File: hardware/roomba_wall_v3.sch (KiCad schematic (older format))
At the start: 15 parts, among them CON1 AVR-ISP-6, IC1 MIC5225-3.3, J1 USB_OTG, J2 JSTPH, J3 JSTPH, Q1 Q_NPN_BEC, U1 ATTINY45-20SU, Y1 8Mhz

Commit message: Schematic for v3 Added a user button mostly Changed to a switch and a battery, like v2 (from Christmas Barrier)
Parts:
- removed C1: 10uF, lib_fp:C_1206, symbol C
- removed IC1: MIC5225-3.3, lib_fp:SOT-23-5_HandSoldering, symbol MIC5225-3.3
- removed J1: USB_OTG, lib_fp:USB_Micro-B_10103594-0001LF, symbol USB_OTG
- removed J3: JSTPH, lib_fp:JST_PH_B2B-PH-SM4-TB_02x2.00mm_Straight, symbol Conn_01x02
- added BT?: Battery_Cell, symbol Battery_Cell
- added R?: 10k, symbol R
- added SW?: On/Off, symbol SW_SPDT
- added SW?: Button, symbol SW_Push
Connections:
- net labels added: SCK/BUTTON, VBAT
- net labels removed: SCK, VBUS
- wire segments 49 -> 40
- no-connect marks 4 -> 1

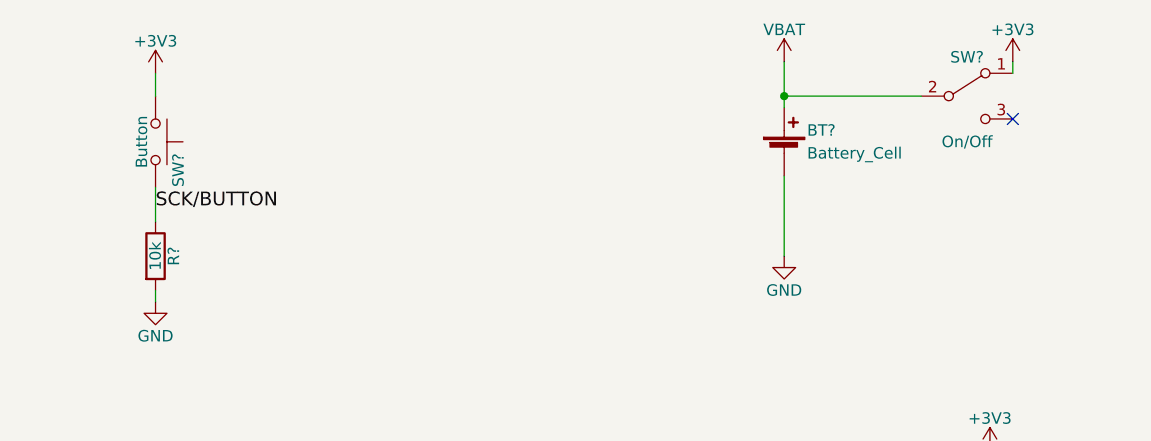
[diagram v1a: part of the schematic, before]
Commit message: Progress on annotating and reassigning footprints I want to use 0805, since they seem the easiest and cheapest to source
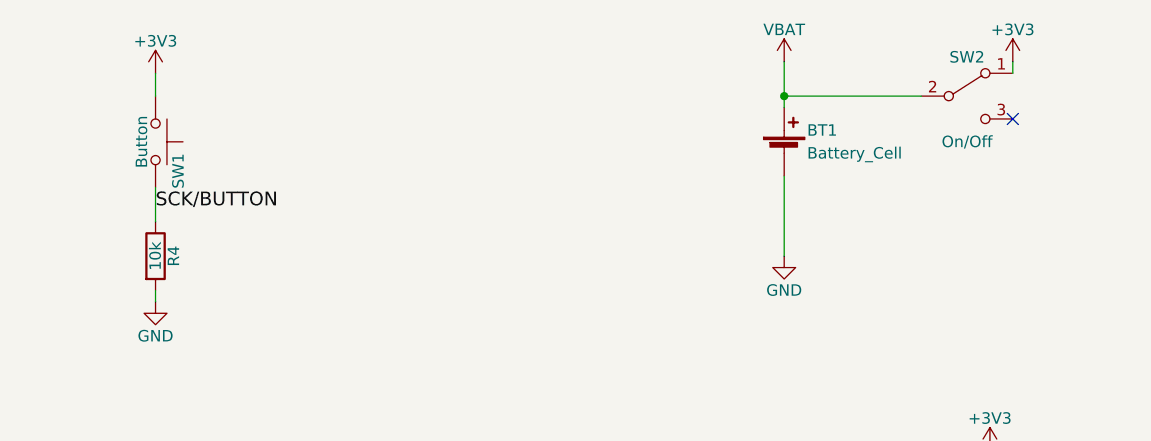
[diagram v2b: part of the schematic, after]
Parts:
- C2: footprint lib_fp:C_1206 -> Capacitors_SMD:C_0805
- D1: footprint lib_fp:LED_1206 -> LEDs:LED_0805
- D2: footprint lib_fp:LED_0603_HandSoldering -> LEDs:LED_0603
- Q1: footprint lib_fp:SOT-23_Handsoldering -> TO_SOT_Packages_SMD:SOT-23
- R1, R2, R3: footprint lib_fp:R_1206 -> Resistors_SMD:R_0805
- R4: renamed from R?; footprint (none) -> Resistors_SMD:R_0805
- gave numbers to parts that had none: 3
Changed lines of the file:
@@
 LIBS:contrib
 LIBS:valves
-LIBS:petezah
-LIBS:petezah-conn
-LIBS:petezah-devices
-LIBS:petezah-ic
-LIBS:petezah-jumpers
-LIBS:petezah-power
-LIBS:roomba_wall_v3-cache
 EELAYER 25 0
 EELAYER END
@@
 RST
 $Comp
-L GND #PWR01
+L GND #PWR10
 U 1 1 5A1C62BB
 P 7300 4100
-F 0 "#PWR01" H 7300 3850 50  0001 C CNN
+F 0 "#PWR10" H 7300 3850 50  0001 C CNN
 F 1 "GND" H 7300 3950 50  0000 C CNN
 F 2 "" H 7300 4100 50  0001 C CNN
@@
 $EndComp
 $Comp
-L +3V3 #PWR02
+L +3V3 #PWR9
 U 1 1 5A1C6304
 P 7300 3200
-F 0 "#PWR02" H 7300 3050 50  0001 C CNN
+F 0 "#PWR9" H 7300 3050 50  0001 C CNN
 F 1 "+3V3" H 7300 3340 50  0000 C CNN
 F 2 "" H 7300 3200 50  0001 C CNN
@@
 $EndComp
 $Comp
-L GND #PWR03
+L GND #PWR6
 U 1 1 5A1C63A0
 P 3950 4350
-F 0 "#PWR03" H 3950 4100 50  0001 C CNN
+F 0 "#PWR6" H 3950 4100 50  0001 C CNN
 F 1 "GND" H 3950 4200 50  0000 C CNN
 F 2 "" H 3950 4350 50  0001 C CNN
@@
 F 0 "R1" V 1330 3550 50  0000 C CNN
 F 1 "560" V 1250 3550 50  0000 C CNN
-F 2 "lib_fp:R_1206" V 1180 3550 50  0001 C CNN
+F 2 "Resistors_SMD:R_0805" V 1180 3550 50  0001 C CNN
 F 3 "" H 1250 3550 50  0001 C CNN
 	1    1250 3550
@@
 F 0 "R2" V 2030 3550 50  0000 C CNN
 F 1 "560" V 1950 3550 50  0000 C CNN
-F 2 "lib_fp:R_1206" V 1880 3550 50  0001 C CNN
+F 2 "Resistors_SMD:R_0805" V 1880 3550 50  0001 C CNN
 F 3 "" H 1950 3550 50  0001 C CNN
 	1    1950 3550
@@
 F 0 "R3" V 2530 3550 50  0000 C CNN
 F 1 "51" V 2450 3550 50  0000 C CNN
-F 2 "lib_fp:R_1206" V 2380 3550 50  0001 C CNN
+F 2 "Resistors_SMD:R_0805" V 2380 3550 50  0001 C CNN
 F 3 "" H 2450 3550 50  0001 C CNN
 	1    2450 3550
@@
 F 0 "D1" H 1250 4300 50  0000 C CNN
 F 1 "LED" H 1250 4100 50  0000 C CNN
-F 2 "lib_fp:LED_1206" H 1250 4200 50  0001 C CNN
+F 2 "LEDs:LED_0805" H 1250 4200 50  0001 C CNN
 F 3 "" H 1250 4200 50  0001 C CNN
 	1    1250 4200
@@
 F 0 "D2" H 2450 4000 50  0000 C CNN
 F 1 "IR_LED" H 2450 3800 50  0000 C CNN
-F 2 "lib_fp:LED_0603_HandSoldering" H 2450 3900 50  0001 C CNN
+F 2 "LEDs:LED_0603" H 2450 3900 50  0001 C CNN
 F 3 "" H 2450 3900 50  0001 C CNN
 	1    2450 3900
@@
 $EndComp
 $Comp
-L +3V3 #PWR04
+L +3V3 #PWR2
 U 1 1 5A1C6749
 P 2450 3100
-F 0 "#PWR04" H 2450 2950 50  0001 C CNN
+F 0 "#PWR2" H 2450 2950 50  0001 C CNN
 F 1 "+3V3" H 2450 3240 50  0000 C CNN
 F 2 "" H 2450 3100 50  0001 C CNN
@@
 $EndComp
 $Comp
-L GND #PWR05
+L GND #PWR1
 U 1 1 5A1C676D
 P 1250 4700
-F 0 "#PWR05" H 1250 4450 50  0001 C CNN
+F 0 "#PWR1" H 1250 4450 50  0001 C CNN
 F 1 "GND" H 1250 4550 50  0000 C CNN
 F 2 "" H 1250 4700 50  0001 C CNN
@@
 $EndComp
 $Comp
-L GND #PWR06
+L GND #PWR3
 U 1 1 5A1C6791
 P 2450 4700
-F 0 "#PWR06" H 2450 4450 50  0001 C CNN
+F 0 "#PWR3" H 2450 4450 50  0001 C CNN
 F 1 "GND" H 2450 4550 50  0000 C CNN
 F 2 "" H 2450 4700 50  0001 C CNN
@@
 RST
 $Comp
-L +3V3 #PWR07
+L +3V3 #PWR15
 U 1 1 5A1C7024
 P 9800 3200
-F 0 "#PWR07" H 9800 3050 50  0001 C CNN
+F 0 "#PWR15" H 9800 3050 50  0001 C CNN
 F 1 "+3V3" H 9800 3340 50  0000 C CNN
 F 2 "" H 9800 3200 50  0001 C CNN
@@
 $EndComp
 $Comp
-L GND #PWR08
+L GND #PWR16
 U 1 1 5A1C704A
 P 9800 4100
-F 0 "#PWR08" H 9800 3850 50  0001 C CNN
+F 0 "#PWR16" H 9800 3850 50  0001 C CNN
 F 1 "GND" H 9800 3950 50  0000 C CNN
 F 2 "" H 9800 4100 50  0001 C CNN
@@
 F 0 "C2" H 7675 3700 50  0000 L CNN
 F 1 "10uF" H 7675 3500 50  0000 L CNN
-F 2 "lib_fp:C_1206" H 7688 3450 50  0001 C CNN
+F 2 "Capacitors_SMD:C_0805" H 7688 3450 50  0001 C CNN
 F 3 "" H 7650 3600 50  0001 C CNN
 	1    7650 3600
@@
 $EndComp
 $Comp
-L GND #PWR013
+L GND #PWR12
 U 1 1 5A1C763D
 P 7650 3750
-F 0 "#PWR013" H 7650 3500 50  0001 C CNN
+F 0 "#PWR12" H 7650 3500 50  0001 C CNN
 F 1 "GND" H 7650 3600 50  0000 C CNN
 F 2 "" H 7650 3750 50  0001 C CNN
@@
 $EndComp
 $Comp
-L +3V3 #PWR017
+L +3V3 #PWR13
 U 1 1 5A1C8097
 P 8400 1550
-F 0 "#PWR017" H 8400 1400 50  0001 C CNN
+F 0 "#PWR13" H 8400 1400 50  0001 C CNN
 F 1 "+3V3" H 8400 1690 50  0000 C CNN
 F 2 "" H 8400 1550 50  0001 C CNN
@@
 $EndComp
 $Comp
-L GND #PWR019
+L GND #PWR14
 U 1 1 5A1C86A4
 P 8400 2350
-F 0 "#PWR019" H 8400 2100 50  0001 C CNN
+F 0 "#PWR14" H 8400 2100 50  0001 C CNN
 F 1 "GND" H 8400 2200 50  0000 C CNN
 F 2 "" H 8400 2350 50  0001 C CNN
@@
 F 0 "Q1" H 2550 4400 50  0000 L CNN
 F 1 "Q_NPN_BEC" H 2550 4300 50  0000 L CNN
-F 2 "lib_fp:SOT-23_Handsoldering" H 2550 4450 50  0001 C CNN
+F 2 "TO_SOT_Packages_SMD:SOT-23" H 2550 4450 50  0001 C CNN
 F 3 "" H 2350 4350 50  0001 C CNN
 	1    2350 4350
@@
 $EndComp
 $Comp
-L Battery_Cell BT?
+L Battery_Cell BT1
 U 1 1 5A96233E
 P 6400 1900
-F 0 "BT?" H 6500 2000 50  0000 L CNN
+F 0 "BT1" H 6500 2000 50  0000 L CNN
 F 1 "Battery_Cell" H 6500 1900 50  0000 L CNN
 F 2 "" V 6400 1960 50  0001 C CNN
@@
 $EndComp
 $Comp
-L VBAT #PWR?
+L VBAT #PWR7
 U 1 1 5A96243B
 P 6400 1500
-F 0 "#PWR?" H 6400 1350 50  0001 C CNN
+F 0 "#PWR7" H 6400 1350 50  0001 C CNN
 F 1 "VBAT" H 6400 1640 50  0000 C CNN
 F 2 "" H 6400 1500 50  0000 C CNN
@@
 	6400 1500 6400 1700
 $Comp
-L GND #PWR?
+L GND #PWR8
 U 1 1 5A962497
 P 6400 2350
-F 0 "#PWR?" H 6400 2100 50  0001 C CNN
+F 0 "#PWR8" H 6400 2100 50  0001 C CNN
 F 1 "GND" H 6400 2200 50  0000 C CNN
 F 2 "" H 6400 2350 50  0001 C CNN
@@
 $EndComp
 $Comp
-L SW_SPDT SW?
+L SW_SPDT SW2
 U 1 1 5A9625C6
 P 7200 1650
-F 0 "SW?" H 7200 1820 50  0000 C CNN
+F 0 "SW2" H 7200 1820 50  0000 C CNN
 F 1 "On/Off" H 7200 1450 50  0000 C CNN
 F 2 "" H 7200 1650 50  0001 C CNN
@@
 Connection ~ 6400 1650
 $Comp
-L +3V3 #PWR?
+L +3V3 #PWR11
 U 1 1 5A9626C7
 P 7400 1500
-F 0 "#PWR?" H 7400 1350 50  0001 C CNN
+F 0 "#PWR11" H 7400 1350 50  0001 C CNN
 F 1 "+3V3" H 7400 1640 50  0000 C CNN
 F 2 "" H 7400 1500 50  0001 C CNN
@@
 NoConn ~ 7400 1750
 $Comp
-L SW_Push SW?
+L SW_Push SW1
 U 1 1 5A9628F7
 P 3650 1850
-F 0 "SW?" H 3700 1950 50  0000 L CNN
+F 0 "SW1" H 3700 1950 50  0000 L CNN
 F 1 "Button" H 3650 1790 50  0000 C CNN
 F 2 "" H 3650 2050 50  0001 C CNN
@@
 $EndComp
 $Comp
-L R R?
+L R R4
 U 1 1 5A962AB2
 P 3650 2350
-F 0 "R?" V 3730 2350 50  0000 C CNN
+F 0 "R4" V 3730 2350 50  0000 C CNN
 F 1 "10k" V 3650 2350 50  0000 C CNN
-F 2 "" V 3580 2350 50  0001 C CNN
+F 2 "Resistors_SMD:R_0805" V 3580 2350 50  0001 C CNN
 F 3 "" H 3650 2350 50  0001 C CNN
 	1    3650 2350
@@
 $EndComp
 $Comp
-L GND #PWR?
+L GND #PWR5
 U 1 1 5A962B09
 P 3650 2550
-F 0 "#PWR?" H 3650 2300 50  0001 C CNN
+F 0 "#PWR5" H 3650 2300 50  0001 C CNN
 F 1 "GND" H 3650 2400 50  0000 C CNN
 F 2 "" H 3650 2550 50  0001 C CNN
@@
 SCK/BUTTON
 $Comp
-L +3V3 #PWR?
+L +3V3 #PWR4
 U 1 1 5A962C2C
 P 3650 1550
-F 0 "#PWR?" H 3650 1400 50  0001 C CNN
+F 0 "#PWR4" H 3650 1400 50  0001 C CNN
 F 1 "+3V3" H 3650 1690 50  0000 C CNN
 F 2 "" H 3650 1550 50  0001 C CNN

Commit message: Updated footprint associations, etc for v3
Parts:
- BT1: footprint (none) -> kicad-libs:CR2032-THRU
- SW1: footprint (none) -> kicad-libs:e-switch-TL-3340-AF160QG
- SW2: footprint (none) -> kicad-libs:SSSS810701
- U1: footprint lib_fp:SOIC-8_5.35x5.40mm_Pitch1.27mm -> kicad-libs:ATtiny45V-10XU-TSSOP-8
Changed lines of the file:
@@
 LIBS:contrib
 LIBS:valves
+LIBS:roomba_wall_v3-cache
 EELAYER 25 0
 EELAYER END
@@
 F 0 "U1" H 4650 4100 50  0000 C CNN
 F 1 "ATTINY45-20SU" H 6800 3300 50  0000 C CNN
-F 2 "lib_fp:SOIC-8_5.35x5.40mm_Pitch1.27mm" H 6750 3700 50  0001 C CIN
+F 2 "kicad-libs:ATtiny45V-10XU-TSSOP-8" H 6750 3700 50  0001 C CIN
 F 3 "" H 5800 3700 50  0001 C CNN
 	1    5800 3700
@@
 RST
 $Comp
-L GND #PWR10
+L GND #PWR01
 U 1 1 5A1C62BB
 P 7300 4100
-F 0 "#PWR10" H 7300 3850 50  0001 C CNN
+F 0 "#PWR01" H 7300 3850 50  0001 C CNN
 F 1 "GND" H 7300 3950 50  0000 C CNN
 F 2 "" H 7300 4100 50  0001 C CNN
@@
 $EndComp
 $Comp
-L +3V3 #PWR9
+L +3V3 #PWR02
 U 1 1 5A1C6304
 P 7300 3200
-F 0 "#PWR9" H 7300 3050 50  0001 C CNN
+F 0 "#PWR02" H 7300 3050 50  0001 C CNN
 F 1 "+3V3" H 7300 3340 50  0000 C CNN
 F 2 "" H 7300 3200 50  0001 C CNN
@@
 $EndComp
 $Comp
-L GND #PWR6
+L GND #PWR03
 U 1 1 5A1C63A0
 P 3950 4350
-F 0 "#PWR6" H 3950 4100 50  0001 C CNN
+F 0 "#PWR03" H 3950 4100 50  0001 C CNN
 F 1 "GND" H 3950 4200 50  0000 C CNN
 F 2 "" H 3950 4350 50  0001 C CNN
@@
 $EndComp
 $Comp
-L +3V3 #PWR2
+L +3V3 #PWR04
 U 1 1 5A1C6749
 P 2450 3100
-F 0 "#PWR2" H 2450 2950 50  0001 C CNN
+F 0 "#PWR04" H 2450 2950 50  0001 C CNN
 F 1 "+3V3" H 2450 3240 50  0000 C CNN
 F 2 "" H 2450 3100 50  0001 C CNN
@@
 $EndComp
 $Comp
-L GND #PWR1
+L GND #PWR05
 U 1 1 5A1C676D
 P 1250 4700
-F 0 "#PWR1" H 1250 4450 50  0001 C CNN
+F 0 "#PWR05" H 1250 4450 50  0001 C CNN
 F 1 "GND" H 1250 4550 50  0000 C CNN
 F 2 "" H 1250 4700 50  0001 C CNN
@@
 $EndComp
 $Comp
-L GND #PWR3
+L GND #PWR06
 U 1 1 5A1C6791
 P 2450 4700
-F 0 "#PWR3" H 2450 4450 50  0001 C CNN
+F 0 "#PWR06" H 2450 4450 50  0001 C CNN
 F 1 "GND" H 2450 4550 50  0000 C CNN
 F 2 "" H 2450 4700 50  0001 C CNN
@@
 RST
 $Comp
-L +3V3 #PWR15
+L +3V3 #PWR07
 U 1 1 5A1C7024
 P 9800 3200
-F 0 "#PWR15" H 9800 3050 50  0001 C CNN
+F 0 "#PWR07" H 9800 3050 50  0001 C CNN
 F 1 "+3V3" H 9800 3340 50  0000 C CNN
 F 2 "" H 9800 3200 50  0001 C CNN
@@
 $EndComp
 $Comp
-L GND #PWR16
+L GND #PWR08
 U 1 1 5A1C704A
 P 9800 4100
-F 0 "#PWR16" H 9800 3850 50  0001 C CNN
+F 0 "#PWR08" H 9800 3850 50  0001 C CNN
 F 1 "GND" H 9800 3950 50  0000 C CNN
 F 2 "" H 9800 4100 50  0001 C CNN
@@
 $EndComp
 $Comp
-L GND #PWR12
+L GND #PWR09
 U 1 1 5A1C763D
 P 7650 3750
-F 0 "#PWR12" H 7650 3500 50  0001 C CNN
+F 0 "#PWR09" H 7650 3500 50  0001 C CNN
 F 1 "GND" H 7650 3600 50  0000 C CNN
 F 2 "" H 7650 3750 50  0001 C CNN
@@
 $EndComp
 $Comp
-L +3V3 #PWR13
+L +3V3 #PWR010
 U 1 1 5A1C8097
 P 8400 1550
-F 0 "#PWR13" H 8400 1400 50  0001 C CNN
+F 0 "#PWR010" H 8400 1400 50  0001 C CNN
 F 1 "+3V3" H 8400 1690 50  0000 C CNN
 F 2 "" H 8400 1550 50  0001 C CNN
@@
 $EndComp
 $Comp
-L GND #PWR14
+L GND #PWR011
 U 1 1 5A1C86A4
 P 8400 2350
-F 0 "#PWR14" H 8400 2100 50  0001 C CNN
+F 0 "#PWR011" H 8400 2100 50  0001 C CNN
 F 1 "GND" H 8400 2200 50  0000 C CNN
 F 2 "" H 8400 2350 50  0001 C CNN
@@
 F 0 "BT1" H 6500 2000 50  0000 L CNN
 F 1 "Battery_Cell" H 6500 1900 50  0000 L CNN
-F 2 "" V 6400 1960 50  0001 C CNN
+F 2 "kicad-libs:CR2032-THRU" V 6400 1960 50  0001 C CNN
 F 3 "" V 6400 1960 50  0001 C CNN
 	1    6400 1900
@@
 $EndComp
 $Comp
-L VBAT #PWR7
+L VBAT #PWR012
 U 1 1 5A96243B
 P 6400 1500
-F 0 "#PWR7" H 6400 1350 50  0001 C CNN
+F 0 "#PWR012" H 6400 1350 50  0001 C CNN
 F 1 "VBAT" H 6400 1640 50  0000 C CNN
 F 2 "" H 6400 1500 50  0000 C CNN
@@
 	6400 1500 6400 1700
 $Comp
-L GND #PWR8
+L GND #PWR013
 U 1 1 5A962497
 P 6400 2350
-F 0 "#PWR8" H 6400 2100 50  0001 C CNN
+F 0 "#PWR013" H 6400 2100 50  0001 C CNN
 F 1 "GND" H 6400 2200 50  0000 C CNN
 F 2 "" H 6400 2350 50  0001 C CNN
@@
 F 0 "SW2" H 7200 1820 50  0000 C CNN
 F 1 "On/Off" H 7200 1450 50  0000 C CNN
-F 2 "" H 7200 1650 50  0001 C CNN
+F 2 "kicad-libs:SSSS810701" H 7200 1650 50  0001 C CNN
 F 3 "" H 7200 1650 50  0001 C CNN
 	1    7200 1650
@@
 Connection ~ 6400 1650
 $Comp
-L +3V3 #PWR11
+L +3V3 #PWR014
 U 1 1 5A9626C7
 P 7400 1500
-F 0 "#PWR11" H 7400 1350 50  0001 C CNN
+F 0 "#PWR014" H 7400 1350 50  0001 C CNN
 F 1 "+3V3" H 7400 1640 50  0000 C CNN
 F 2 "" H 7400 1500 50  0001 C CNN
@@
 F 0 "SW1" H 3700 1950 50  0000 L CNN
 F 1 "Button" H 3650 1790 50  0000 C CNN
-F 2 "" H 3650 2050 50  0001 C CNN
+F 2 "kicad-libs:e-switch-TL-3340-AF160QG" H 3650 2050 50  0001 C CNN
 F 3 "" H 3650 2050 50  0001 C CNN
 	1    3650 1850
@@
 $EndComp
 $Comp
-L GND #PWR5
+L GND #PWR015
 U 1 1 5A962B09
 P 3650 2550
-F 0 "#PWR5" H 3650 2300 50  0001 C CNN
+F 0 "#PWR015" H 3650 2300 50  0001 C CNN
 F 1 "GND" H 3650 2400 50  0000 C CNN
 F 2 "" H 3650 2550 50  0001 C CNN
@@
 SCK/BUTTON
 $Comp
-L +3V3 #PWR4
+L +3V3 #PWR016
 U 1 1 5A962C2C
 P 3650 1550
-F 0 "#PWR4" H 3650 1400 50  0001 C CNN
+F 0 "#PWR016" H 3650 1400 50  0001 C CNN
 F 1 "+3V3" H 3650 1690 50  0000 C CNN
 F 2 "" H 3650 1550 50  0001 C CNN

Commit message: Fix fp archive pointers
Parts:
- BT1: footprint kicad-libs:CR2032-THRU -> lib_fp:CR2032-THRU
- C2: footprint Capacitors_SMD:C_0805 -> lib_fp:C_0805
- D1: footprint LEDs:LED_0805 -> lib_fp:LED_0805
- D2: footprint LEDs:LED_0603 -> lib_fp:LED_0603
- Q1: footprint TO_SOT_Packages_SMD:SOT-23 -> lib_fp:SOT-23
- R1, R2, R3, R4: footprint Resistors_SMD:R_0805 -> lib_fp:R_0805
- SW1: footprint kicad-libs:e-switch-TL-3340-AF160QG -> lib_fp:e-switch-TL-3340-AF160QG
- SW2: footprint kicad-libs:SSSS810701 -> lib_fp:SSSS810701
- U1: footprint kicad-libs:ATtiny45V-10XU-TSSOP-8 -> lib_fp:ATtiny45V-10XU-TSSOP-8
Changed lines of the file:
@@
 Sheet 1 1
 Title "Roomba Wall V3"
-Date "2018-02-27"
+Date "2018-03-03"
 Rev "A"
 Comp "Petezah"
@@
 F 0 "U1" H 4650 4100 50  0000 C CNN
 F 1 "ATTINY45-20SU" H 6800 3300 50  0000 C CNN
-F 2 "kicad-libs:ATtiny45V-10XU-TSSOP-8" H 6750 3700 50  0001 C CIN
+F 2 "lib_fp:ATtiny45V-10XU-TSSOP-8" H 6750 3700 50  0001 C CIN
 F 3 "" H 5800 3700 50  0001 C CNN
 	1    5800 3700
@@
 F 0 "R1" V 1330 3550 50  0000 C CNN
 F 1 "560" V 1250 3550 50  0000 C CNN
-F 2 "Resistors_SMD:R_0805" V 1180 3550 50  0001 C CNN
+F 2 "lib_fp:R_0805" V 1180 3550 50  0001 C CNN
 F 3 "" H 1250 3550 50  0001 C CNN
 	1    1250 3550
@@
 F 0 "R2" V 2030 3550 50  0000 C CNN
 F 1 "560" V 1950 3550 50  0000 C CNN
-F 2 "Resistors_SMD:R_0805" V 1880 3550 50  0001 C CNN
+F 2 "lib_fp:R_0805" V 1880 3550 50  0001 C CNN
 F 3 "" H 1950 3550 50  0001 C CNN
 	1    1950 3550
@@
 F 0 "R3" V 2530 3550 50  0000 C CNN
 F 1 "51" V 2450 3550 50  0000 C CNN
-F 2 "Resistors_SMD:R_0805" V 2380 3550 50  0001 C CNN
+F 2 "lib_fp:R_0805" V 2380 3550 50  0001 C CNN
 F 3 "" H 2450 3550 50  0001 C CNN
 	1    2450 3550
@@
 F 0 "D1" H 1250 4300 50  0000 C CNN
 F 1 "LED" H 1250 4100 50  0000 C CNN
-F 2 "LEDs:LED_0805" H 1250 4200 50  0001 C CNN
+F 2 "lib_fp:LED_0805" H 1250 4200 50  0001 C CNN
 F 3 "" H 1250 4200 50  0001 C CNN
 	1    1250 4200
@@
 F 0 "D2" H 2450 4000 50  0000 C CNN
 F 1 "IR_LED" H 2450 3800 50  0000 C CNN
-F 2 "LEDs:LED_0603" H 2450 3900 50  0001 C CNN
+F 2 "lib_fp:LED_0603" H 2450 3900 50  0001 C CNN
 F 3 "" H 2450 3900 50  0001 C CNN
 	1    2450 3900
@@
 F 0 "C2" H 7675 3700 50  0000 L CNN
 F 1 "10uF" H 7675 3500 50  0000 L CNN
-F 2 "Capacitors_SMD:C_0805" H 7688 3450 50  0001 C CNN
+F 2 "lib_fp:C_0805" H 7688 3450 50  0001 C CNN
 F 3 "" H 7650 3600 50  0001 C CNN
 	1    7650 3600
@@
 F 0 "Q1" H 2550 4400 50  0000 L CNN
 F 1 "Q_NPN_BEC" H 2550 4300 50  0000 L CNN
-F 2 "TO_SOT_Packages_SMD:SOT-23" H 2550 4450 50  0001 C CNN
+F 2 "lib_fp:SOT-23" H 2550 4450 50  0001 C CNN
 F 3 "" H 2350 4350 50  0001 C CNN
 	1    2350 4350
@@
 F 0 "BT1" H 6500 2000 50  0000 L CNN
 F 1 "Battery_Cell" H 6500 1900 50  0000 L CNN
-F 2 "kicad-libs:CR2032-THRU" V 6400 1960 50  0001 C CNN
+F 2 "lib_fp:CR2032-THRU" V 6400 1960 50  0001 C CNN
 F 3 "" V 6400 1960 50  0001 C CNN
 	1    6400 1900
@@
 F 0 "SW2" H 7200 1820 50  0000 C CNN
 F 1 "On/Off" H 7200 1450 50  0000 C CNN
-F 2 "kicad-libs:SSSS810701" H 7200 1650 50  0001 C CNN
+F 2 "lib_fp:SSSS810701" H 7200 1650 50  0001 C CNN
 F 3 "" H 7200 1650 50  0001 C CNN
 	1    7200 1650
@@
 F 0 "SW1" H 3700 1950 50  0000 L CNN
 F 1 "Button" H 3650 1790 50  0000 C CNN
-F 2 "kicad-libs:e-switch-TL-3340-AF160QG" H 3650 2050 50  0001 C CNN
+F 2 "lib_fp:e-switch-TL-3340-AF160QG" H 3650 2050 50  0001 C CNN
 F 3 "" H 3650 2050 50  0001 C CNN
 	1    3650 1850
@@
 F 0 "R4" V 3730 2350 50  0000 C CNN
 F 1 "10k" V 3650 2350 50  0000 C CNN
-F 2 "Resistors_SMD:R_0805" V 3580 2350 50  0001 C CNN
+F 2 "lib_fp:R_0805" V 3580 2350 50  0001 C CNN
 F 3 "" H 3650 2350 50  0001 C CNN
 	1    3650 2350

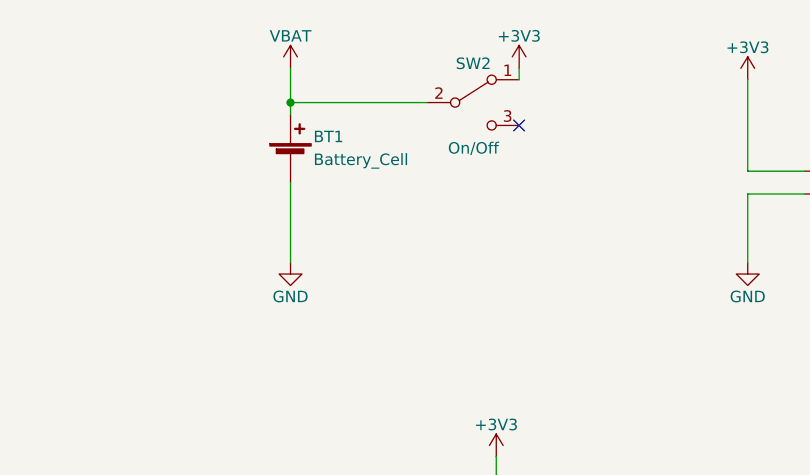
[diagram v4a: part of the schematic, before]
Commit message: Fix all ERC errors
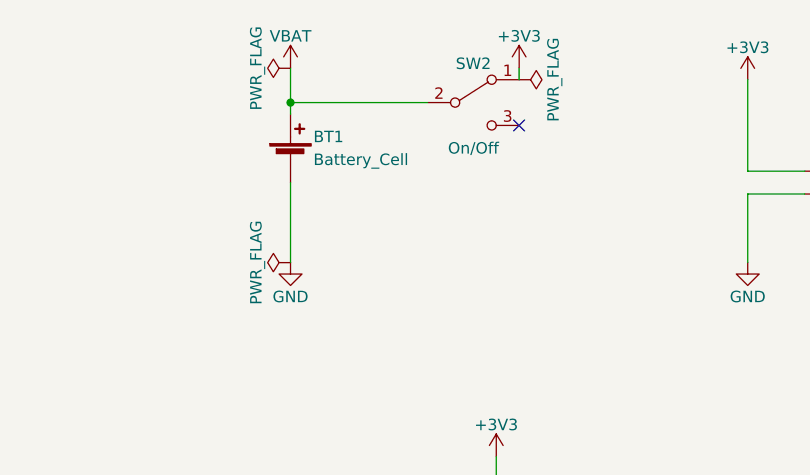
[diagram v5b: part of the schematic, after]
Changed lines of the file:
@@
 Wire Wire Line
 	3650 1650 3650 1550
+$Comp
+L PWR_FLAG #FLG017
+U 1 1 5A9B0C29
+P 6400 2350
+F 0 "#FLG017" H 6400 2425 50  0001 C CNN
+F 1 "PWR_FLAG" H 6400 2500 50  0000 C CNN
+F 2 "" H 6400 2350 50  0001 C CNN
+F 3 "" H 6400 2350 50  0001 C CNN
+	1    6400 2350
+	0    -1   -1   0
+$EndComp
+$Comp
+L PWR_FLAG #FLG018
+U 1 1 5A9B0CF1
+P 6400 1500
+F 0 "#FLG018" H 6400 1575 50  0001 C CNN
+F 1 "PWR_FLAG" H 6400 1650 50  0000 C CNN
+F 2 "" H 6400 1500 50  0001 C CNN
+F 3 "" H 6400 1500 50  0001 C CNN
+	1    6400 1500
+	0    -1   -1   0
+$EndComp
+$Comp
+L PWR_FLAG #FLG019
+U 1 1 5A9B0F1D
+P 7400 1550
+F 0 "#FLG019" H 7400 1625 50  0001 C CNN
+F 1 "PWR_FLAG" H 7400 1700 50  0000 C CNN
+F 2 "" H 7400 1550 50  0001 C CNN
+F 3 "" H 7400 1550 50  0001 C CNN
+	1    7400 1550
+	0    1    1    0
+$EndComp
 $EndSCHEMATC
